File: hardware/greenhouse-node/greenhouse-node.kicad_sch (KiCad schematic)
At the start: 35 parts, among them J1 Conn_01x12_Male, J2 Conn_01x02_Male, J3 Conn_01x02_Male, J4 Conn_01x02_Male, J5 Conn_01x04_Male, J6 RX_PinHeader_1x04_P2.54mm, J7 TX_PinHeader_1x04_P2.54mm, Q1 BC549C, U1 ATtiny84A-P, U2 L7805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

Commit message: Add value to PCB
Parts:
- Y1: renamed from Y?; value Crystal_Small -> 8MHz; footprint (none) -> Crystal:Crystal_HC49-U_Vertical
- gave numbers to parts that had none: 2
- renumbered C5 to C7, J4 to J2, J2 to J3, J3 to J4

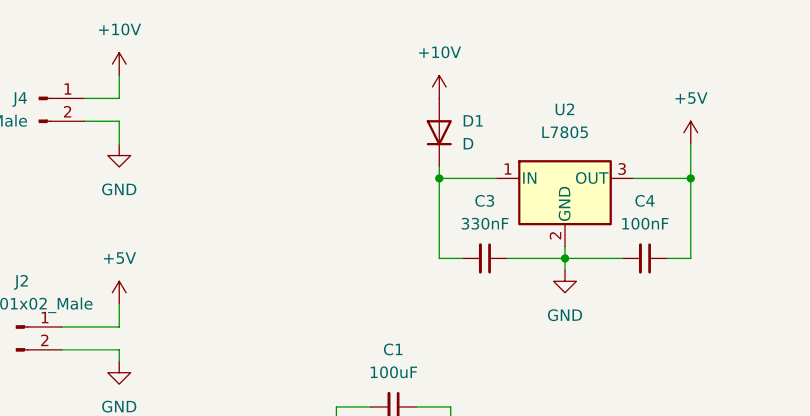
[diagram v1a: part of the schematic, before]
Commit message: Repositioned DIPs
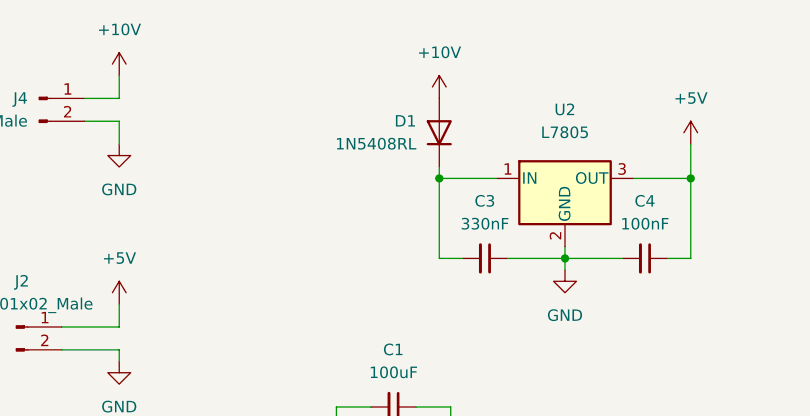
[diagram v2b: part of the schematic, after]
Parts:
- D1: value D -> 1N5408RL
- Y1: footprint Crystal:Crystal_HC49-U_Vertical -> Crystal:Crystal_HC49-4H_Vertical
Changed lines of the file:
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@@
   (symbol (lib_id "Device:D") (at 92.71 38.1 90) (unit 1)
     (in_bom yes) (on_board yes) (fields_autoplaced)
-    (property "Reference" "D1" (id 0) (at 95.25 36.8299 90)
-      (effects (font (size 1.27 1.27)) (justify right))
-    )
-    (property "Value" "D" (id 1) (at 95.25 39.3699 90)
-      (effects (font (size 1.27 1.27)) (justify right))
+    (property "Reference" "D1" (id 0) (at 90.17 36.8299 90)
+      (effects (font (size 1.27 1.27)) (justify left))
+    )
+    (property "Value" "1N5408RL" (id 1) (at 90.17 39.3699 90)
+      (effects (font (size 1.27 1.27)) (justify left))
     )
     (property "Footprint" "Diode_THT:D_A-405_P7.62mm_Horizontal" (id 2) (at 92.71 38.1 0)
@@
       (effects (font (size 1.27 1.27)) (justify left))
     )
-    (property "Footprint" "Crystal:Crystal_HC49-U_Vertical" (id 2) (at 130.81 139.7 0)
+    (property "Footprint" "Crystal:Crystal_HC49-4H_Vertical" (id 2) (at 130.81 139.7 0)
       (effects (font (size 1.27 1.27)) hide)
     )
@@
     )
     (path "/2398c74e-bdaf-4913-b648-f4d9cb68ee90"
-      (reference "D1") (unit 1) (value "D") (footprint "Diode_THT:D_A-405_P7.62mm_Horizontal")
+      (reference "D1") (unit 1) (value "1N5408RL") (footprint "Diode_THT:D_A-405_P7.62mm_Horizontal")
     )
     (path "/51b7deb3-d546-4266-aa92-b89ded074dd4"
@@
     )
     (path "/77646657-5d5b-4281-a7b7-2c11ea23e48c"
-      (reference "Y1") (unit 1) (value "8MHz") (footprint "Crystal:Crystal_HC49-U_Vertical")
-    )
-  )
+      (reference "Y1") (unit 1) (value "8MHz") (footprint "Crystal:Crystal_HC49-4H_Vertical")
+    )
+  )

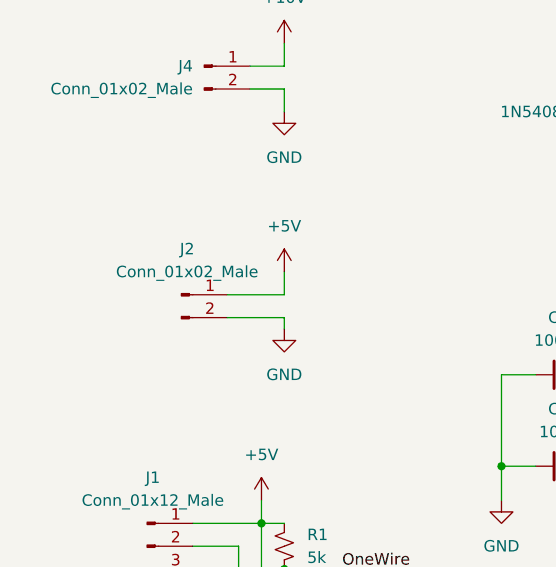
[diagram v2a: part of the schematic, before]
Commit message: Swapped GND/PWR for IC programming connector
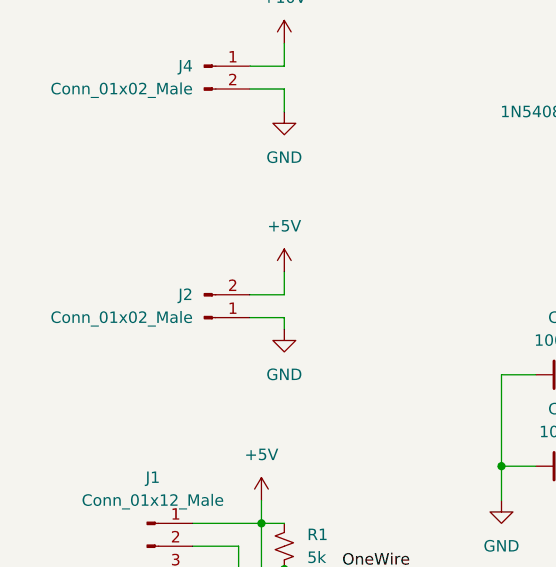
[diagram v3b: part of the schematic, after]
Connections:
- net +5V: now also J2.2 (Pin_2); no longer J2.1 (Pin_1)
- net GND: now also J2.1 (Pin_1); no longer J2.2 (Pin_2)
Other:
- moved on the sheet: J2
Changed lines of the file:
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@@
+    (stroke (width 0) (type default) (color 0 0 0 0))
+  )
+  (wire (pts (xy 57.15 57.15) (xy 57.15 59.69))
     (stroke (width 0) (type default) (color 0 0 0 0))
   )
@@
     (stroke (width 0) (type default) (color 0 0 0 0))
   )
-  (wire (pts (xy 57.15 57.15) (xy 57.15 59.69))
-    (stroke (width 0) (type default) (color 0 0 0 0))
-  )
   (wire (pts (xy 179.07 43.18) (xy 179.07 33.02))
     (stroke (width 0) (type default) (color 0 0 0 0))
@@
     (stroke (width 0) (type default) (color 0 0 0 0))
   )
+  (wire (pts (xy 57.15 59.69) (xy 53.34 59.69))
+    (stroke (width 0) (type default) (color 0 0 0 0))
+  )
   (wire (pts (xy 116.84 104.14) (xy 130.81 104.14))
     (stroke (width 0) (type default) (color 0 0 0 0))
@@
     (stroke (width 0) (type default) (color 0 0 0 0))
   )
-  (wire (pts (xy 50.8 62.23) (xy 57.15 62.23))
-    (stroke (width 0) (type default) (color 0 0 0 0))
-  )
   (wire (pts (xy 92.71 43.18) (xy 99.06 43.18))
     (stroke (width 0) (type default) (color 0 0 0 0))
@@
     (stroke (width 0) (type default) (color 0 0 0 0))
   )
-  (wire (pts (xy 57.15 59.69) (xy 50.8 59.69))
-    (stroke (width 0) (type default) (color 0 0 0 0))
-  )
   (wire (pts (xy 118.11 52.07) (xy 120.65 52.07))
     (stroke (width 0) (type default) (color 0 0 0 0))
@@
     (stroke (width 0) (type default) (color 0 0 0 0))
   )
+  (wire (pts (xy 53.34 62.23) (xy 57.15 62.23))
+    (stroke (width 0) (type default) (color 0 0 0 0))
+  )
   (wire (pts (xy 54.61 100.33) (xy 46.99 100.33))
     (stroke (width 0) (type default) (color 0 0 0 0))
@@
     (stroke (width 0) (type default) (color 0 0 0 0))
   )
+  (wire (pts (xy 57.15 62.23) (xy 57.15 63.5))
+    (stroke (width 0) (type default) (color 0 0 0 0))
+  )
   (wire (pts (xy 106.68 52.07) (xy 113.03 52.07))
     (stroke (width 0) (type default) (color 0 0 0 0))
@@
   )
   (wire (pts (xy 218.44 50.8) (xy 238.76 50.8))
-    (stroke (width 0) (type default) (color 0 0 0 0))
-  )
-  (wire (pts (xy 57.15 62.23) (xy 57.15 63.5))
     (stroke (width 0) (type default) (color 0 0 0 0))
   )
@@
     (pin "1")
   )
-  (symbol (lib_id "power:+5V") (at 57.15 57.15 0) (mirror y) (unit 1)
-    (in_bom yes) (on_board yes) (fields_autoplaced)
-    (property "Reference" "#PWR06" (id 0) (at 57.15 60.96 0)
-      (effects (font (size 1.27 1.27)) hide)
-    )
-    (property "Value" "+5V" (id 1) (at 57.15 52.07 0))
-    (property "Footprint" "" (id 2) (at 57.15 57.15 0)
-      (effects (font (size 1.27 1.27)) hide)
-    )
-    (property "Datasheet" "" (id 3) (at 57.15 57.15 0)
-      (effects (font (size 1.27 1.27)) hide)
-    )
-    (pin "1")
-  )
   (symbol (lib_id "power:GND") (at 52.07 116.84 0) (unit 1)
     (in_bom yes) (on_board yes) (fields_autoplaced)
@@
     (pin "2")
   )
+  (symbol (lib_id "power:GND") (at 57.15 63.5 0) (unit 1)
+    (in_bom yes) (on_board yes) (fields_autoplaced)
+    (property "Reference" "#PWR?" (id 0) (at 57.15 69.85 0)
+      (effects (font (size 1.27 1.27)) hide)
+    )
+    (property "Value" "GND" (id 1) (at 57.15 68.58 0))
+    (property "Footprint" "" (id 2) (at 57.15 63.5 0)
+      (effects (font (size 1.27 1.27)) hide)
+    )
+    (property "Datasheet" "" (id 3) (at 57.15 63.5 0)
+      (effects (font (size 1.27 1.27)) hide)
+    )
+    (pin "1")
+  )
   (symbol (lib_id "power:GND") (at 179.07 67.31 0) (unit 1)
     (in_bom yes) (on_board yes) (fields_autoplaced)
@@
     )
     (property "Datasheet" "" (id 3) (at 106.68 53.34 0)
-      (effects (font (size 1.27 1.27)) hide)
-    )
-    (pin "1")
-  )
-  (symbol (lib_id "power:GND") (at 57.15 63.5 0) (unit 1)
-    (in_bom yes) (on_board yes) (fields_autoplaced)
-    (property "Reference" "#PWR07" (id 0) (at 57.15 69.85 0)
-      (effects (font (size 1.27 1.27)) hide)
-    )
-    (property "Value" "GND" (id 1) (at 57.15 68.58 0))
-    (property "Footprint" "" (id 2) (at 57.15 63.5 0)
-      (effects (font (size 1.27 1.27)) hide)
-    )
-    (property "Datasheet" "" (id 3) (at 57.15 63.5 0)
       (effects (font (size 1.27 1.27)) hide)
     )
@@
     (pin "1")
   )
+  (symbol (lib_id "power:+5V") (at 57.15 57.15 0) (mirror y) (unit 1)
+    (in_bom yes) (on_board yes) (fields_autoplaced)
+    (property "Reference" "#PWR?" (id 0) (at 57.15 60.96 0)
+      (effects (font (size 1.27 1.27)) hide)
+    )
+    (property "Value" "+5V" (id 1) (at 57.15 52.07 0))
+    (property "Footprint" "" (id 2) (at 57.15 57.15 0)
+      (effects (font (size 1.27 1.27)) hide)
+    )
+    (property "Datasheet" "" (id 3) (at 57.15 57.15 0)
+      (effects (font (size 1.27 1.27)) hide)
+    )
+    (pin "1")
+  )
   (symbol (lib_id "Device:LED_Small") (at 163.83 63.5 180) (unit 1)
     (in_bom yes) (on_board yes) (fields_autoplaced)
@@
     (pin "1")
   )
-  (symbol (lib_id "Connector:Conn_01x02_Male") (at 45.72 59.69 0) (unit 1)
-    (in_bom yes) (on_board yes) (fields_autoplaced)
-    (property "Reference" "J2" (id 0) (at 46.355 54.61 0))
-    (property "Value" "Conn_01x02_Male" (id 1) (at 46.355 57.15 0))
-    (property "Footprint" "Connector_JST:JST_XH_B2B-XH-A_1x02_P2.50mm_Vertical" (id 2) (at 45.72 59.69 0)
-      (effects (font (size 1.27 1.27)) hide)
-    )
-    (property "Datasheet" "~" (id 3) (at 45.72 59.69 0)
+  (symbol (lib_id "Connector:Conn_01x02_Male") (at 48.26 62.23 0) (mirror x) (unit 1)
+    (in_bom yes) (on_board yes) (fields_autoplaced)
+    (property "Reference" "J2" (id 0) (at 46.99 59.6899 0)
+      (effects (font (size 1.27 1.27)) (justify right))
+    )
+    (property "Value" "Conn_01x02_Male" (id 1) (at 46.99 62.2299 0)
+      (effects (font (size 1.27 1.27)) (justify right))
+    )
+    (property "Footprint" "Connector_JST:JST_XH_B2B-XH-A_1x02_P2.50mm_Vertical" (id 2) (at 48.26 62.23 0)
+      (effects (font (size 1.27 1.27)) hide)
+    )
+    (property "Datasheet" "~" (id 3) (at 48.26 62.23 0)
       (effects (font (size 1.27 1.27)) hide)
     )
@@
       (reference "#PWR05") (unit 1) (value "GND") (footprint "")
     )
-    (path "/11f1bdc8-089d-4d89-9a9a-949794263e1a"
-      (reference "#PWR06") (unit 1) (value "+5V") (footprint "")
-    )
-    (path "/5a865d92-6efb-4419-b7f5-ea76dd77de1d"
-      (reference "#PWR07") (unit 1) (value "GND") (footprint "")
-    )
     (path "/11bb6fcb-9ef6-4e12-9d6b-33df57416559"
       (reference "#PWR08") (unit 1) (value "GND") (footprint "")
@@
       (reference "#PWR026") (unit 1) (value "GND") (footprint "")
     )
+    (path "/23b24f1a-0314-4640-ad02-55d3e4d235a9"
+      (reference "#PWR?") (unit 1) (value "GND") (footprint "")
+    )
+    (path "/be0a22b0-538f-47bb-8d75-a8ed627b0f03"
+      (reference "#PWR?") (unit 1) (value "+5V") (footprint "")
+    )
     (path "/695ccbcc-4a44-4a1f-b5e4-e7c0459755d8"

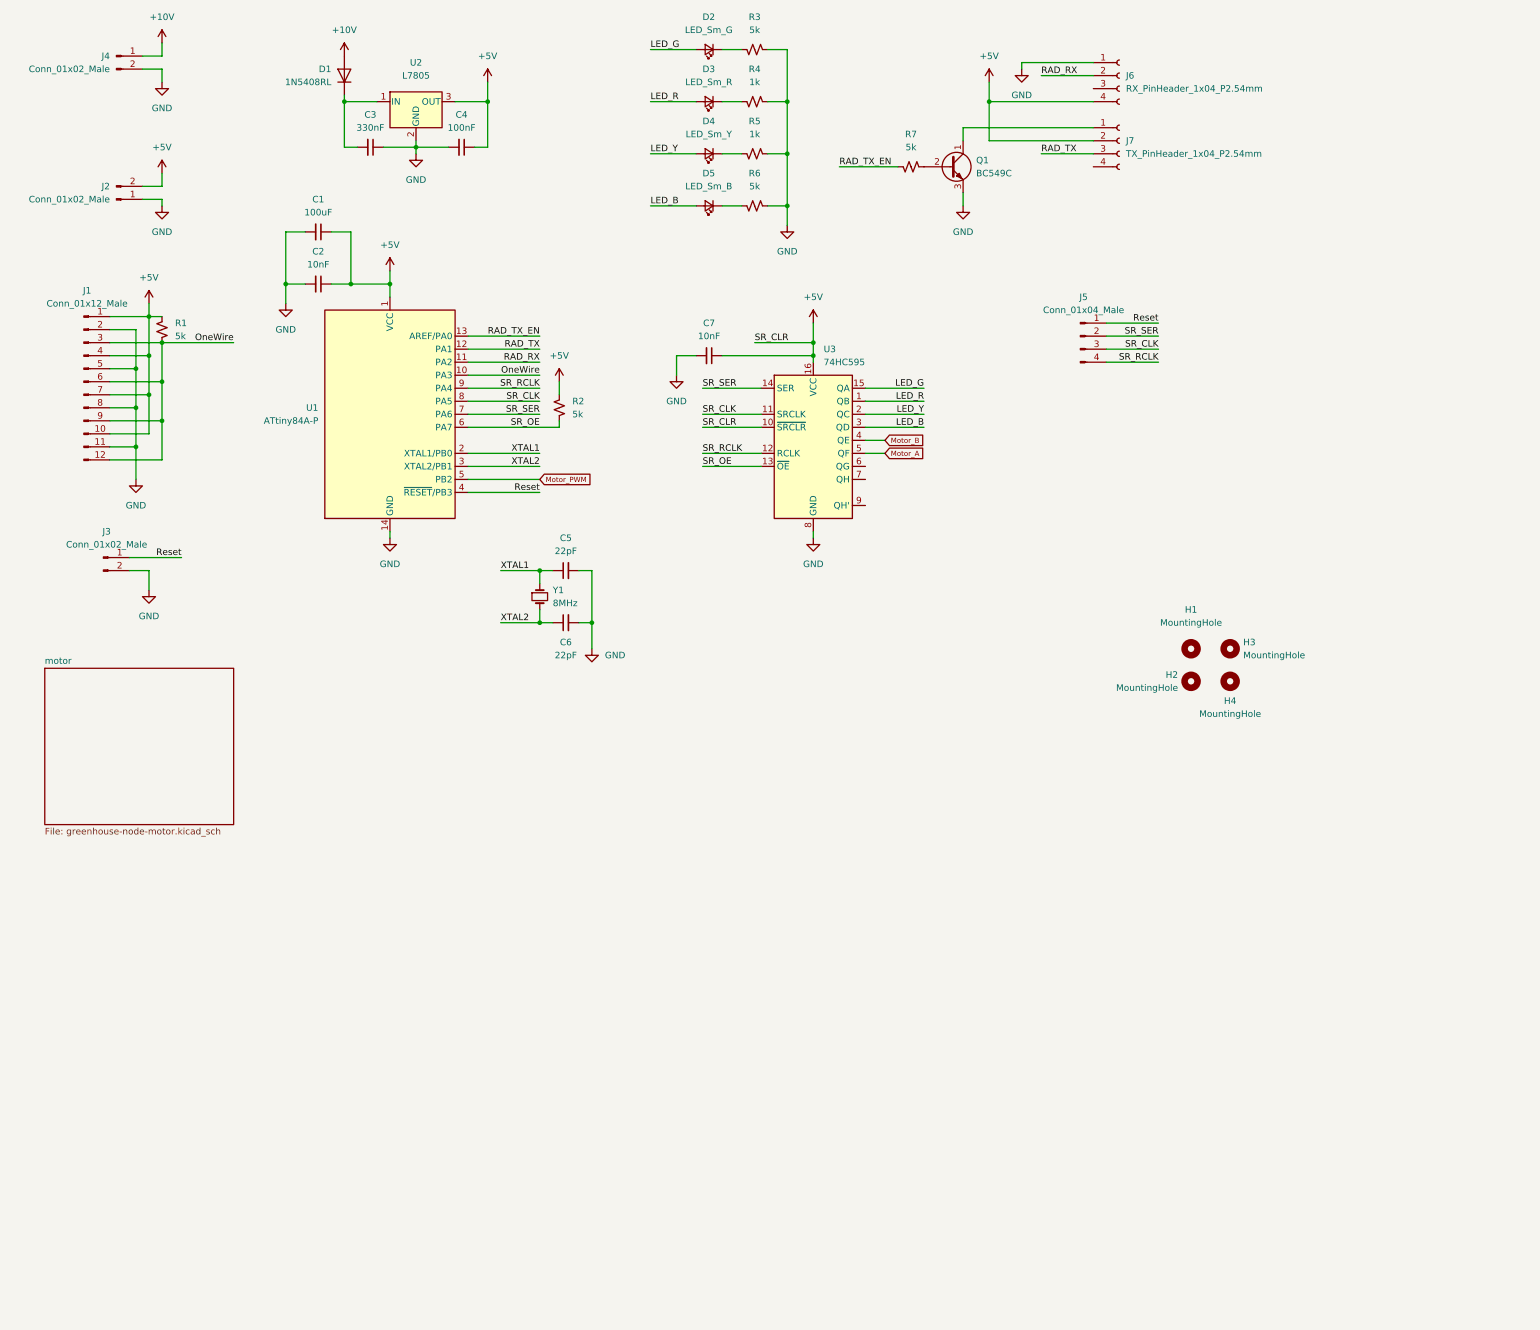
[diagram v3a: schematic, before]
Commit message: Reorganize schematics
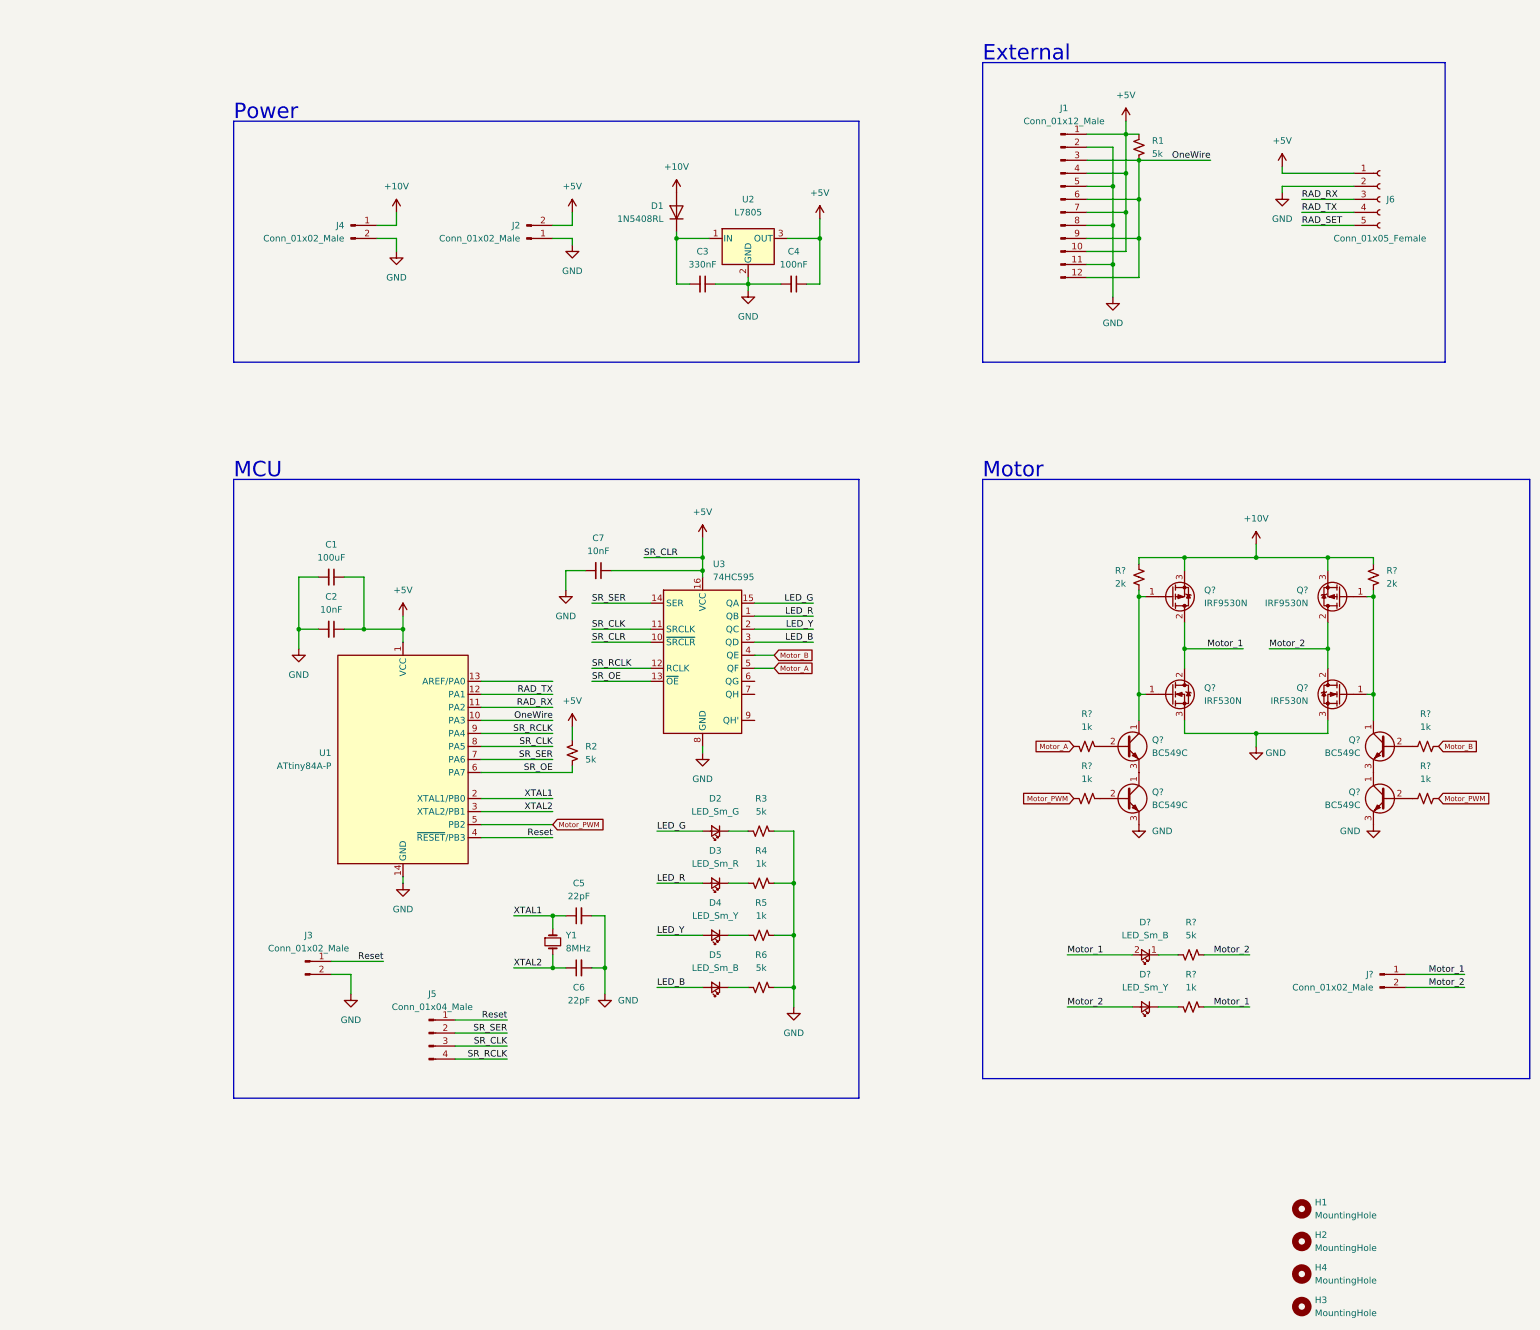
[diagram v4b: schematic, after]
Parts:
- removed J7: TX_PinHeader_1x04_P2.54mm, Connector_PinSocket_2.54mm:PinSocket_1x04_P2.54mm_Vertical, symbol Connector:Conn_01x04_Female
- removed Q1: BC549C, Package_TO_SOT_THT:TO-92_Inline, symbol Transistor_BJT:BC549
- removed R7: 5k, Resistor_THT:R_Axial_DIN0204_L3.6mm_D1.6mm_P7.62mm_Horizontal, symbol Device:R_Small_US
- added D?: LED_Sm_B, LED_THT:LED_D3.0mm, symbol Device:LED_Small
- added D?: LED_Sm_Y, LED_THT:LED_D3.0mm, symbol Device:LED_Small
- added J?: Conn_01x02_Male, Connector_Molex:Molex_KK-396_A-41791-0002_1x02_P3.96mm_Vertical, symbol Connector:Conn_01x02_Male
- added Q? (x4): BC549C, Package_TO_SOT_THT:TO-92_Inline, symbol Transistor_BJT:BC549
- added Q? (x2): IRF9530N, Package_TO_SOT_THT:TO-220-3_Horizontal_TabDown, symbol Transistor_FET:IRF9540N
- added Q? (x2): IRF530N, Package_TO_SOT_THT:TO-220-3_Horizontal_TabDown, symbol Transistor_FET:IRF540N
- added R?: 5k, Resistor_THT:R_Axial_DIN0204_L3.6mm_D1.6mm_P7.62mm_Horizontal, symbol Device:R_Small_US
- added R? (x5): 1k, Resistor_THT:R_Axial_DIN0204_L3.6mm_D1.6mm_P7.62mm_Horizontal, symbol Device:R_Small_US
- added R? (x2): 2k, Resistor_THT:R_Axial_DIN0204_L3.6mm_D1.6mm_P7.62mm_Horizontal, symbol Device:R_Small_US
- J6: value RX_PinHeader_1x04_P2.54mm -> Conn_01x05_Female; footprint Connector_PinSocket_2.54mm:PinSocket_1x04_P2.54mm_Vertical -> Connector_PinSocket_2.54mm:PinSocket_1x05_P2.54mm_Vertical; symbol Connector:Conn_01x04_Female -> Connector:Conn_01x05_Female
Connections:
- net +10V: now also Q?.3 (S), Q?.3 (S), R?.2, R?.2
- net +5V: now also J6.1 (Pin_1); no longer J6.4 (Pin_4)
- net GND: now also J6.2 (Pin_2), Q?.3 (E), Q?.3 (E), Q?.3 (S), Q?.3 (S); no longer J6.1 (Pin_1)
- net Motor_A: now also R?.2
- net Motor_B: now also R?.2
- net Motor_PWM: now also R?.2, R?.2
- net RAD_RX: now also J6.3 (Pin_3); no longer J6.2 (Pin_2)
- net RAD_TX: now also J6.4 (Pin_4)
- net RAD_TX_EN: no longer names the net of U1.13 (AREF/PA0)
- new net: D?.1 (K), R?.2 (x2)
- new net: Q?.1 (C), Q?.1 (G), Q?.1 (G), R?.1 (x2)
- new net: Q?.2 (B), R?.1 (x4)
- new net: Q?.1 (C), Q?.3 (E) (x2)
- new net Motor_1: D?.2 (A), J?.1 (Pin_1), Q?.2 (D), Q?.2 (D), R?.1
- new net Motor_2: D?.2 (A), J?.2 (Pin_2), Q?.2 (D), Q?.2 (D), R?.1
- new net RAD_SET: J6.5 (Pin_5)
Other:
- removed sheet motor
- note added: "External"
- note added: "MCU"
- note added: "Motor"
- note added: "Power"
- moved on the sheet: C1, C2, C3, C4, C5, C6, C7, D1, D2, D3, D4, D5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
